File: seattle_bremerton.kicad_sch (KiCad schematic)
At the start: 31 parts

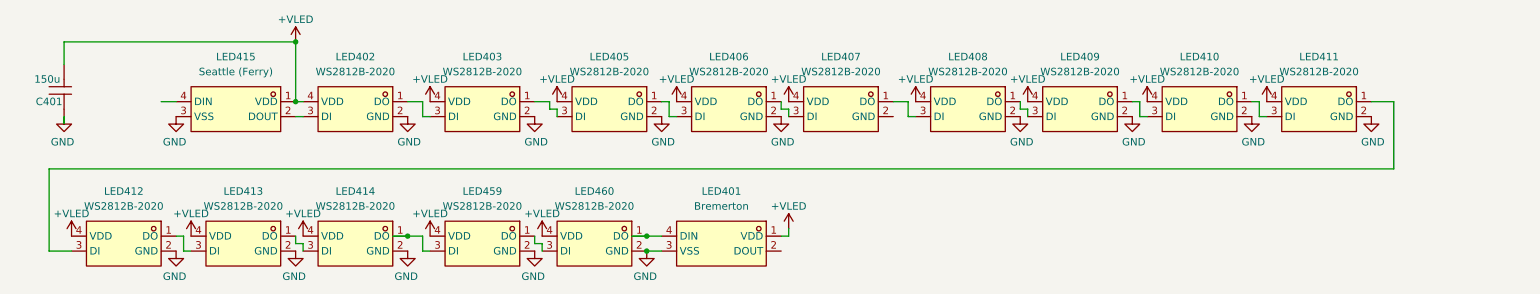
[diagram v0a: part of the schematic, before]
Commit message: checkpoint before stopping double routing
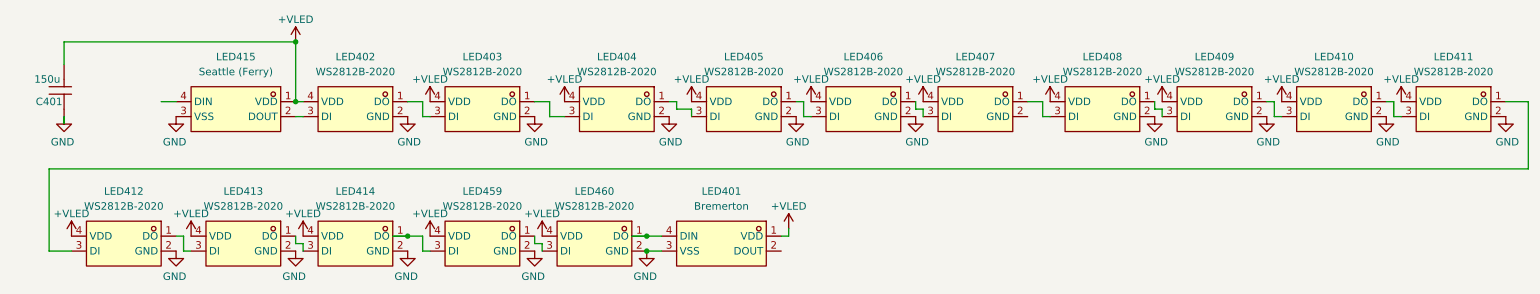
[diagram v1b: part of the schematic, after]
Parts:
- added LED404: WS2812B-2020, EasyEDA:LED-SMD_4P-L2.0-W2.0-TL_WS2812B-2020, symbol EasyEDA:WS2812B-2020
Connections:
- net +VLED: now also LED404.4 (VDD)
- net GND: now also LED404.2 (GND)
- net at LED403.1 (DO): now also LED404.3 (DI); no longer LED405.3 (DI)
- new net: LED404.1 (DO), LED405.3 (DI)
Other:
- moved on the sheet: LED405, LED406, LED407, LED408, LED409, LED410, LED411

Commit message: single ferry track checkpoint
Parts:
- removed LED419, LED430, LED448, LED449, LED450, LED451, LED452, LED453, LED454, LED455, LED456, LED457, LED461, LED462: WS2812B-2020, EasyEDA:LED-SMD_4P-L2.0-W2.0-TL_WS2812B-2020, symbol EasyEDA:WS2812B-2020

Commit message: checkpoint before label plugin
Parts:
- added LED461, LED462: WS2812B-2020, EasyEDA:LED-SMD_4P-L2.0-W2.0-TL_WS2812B-2020, symbol EasyEDA:WS2812B-2020
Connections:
- net +VLED: now also LED461.4 (VDD), LED462.4 (VDD)
- net GND: now also LED461.2 (GND), LED462.2 (GND)
- net at LED460.1 (DO): now also LED461.3 (DI); no longer LED401.4 (DIN)
- new net: LED461.1 (DO), LED462.3 (DI)
- new net: LED401.4 (DIN), LED462.1 (DO)

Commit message: Add rail labels
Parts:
- renumbered LED415 to LED701, LED402 to LED702, LED403 to LED703, LED404 to LED704, LED405 to LED705, LED406 to LED706, LED407 to LED707, LED408 to LED708, LED409 to LED709, LED410 to LED710, LED411 to LED711, LED412 to LED712, LED413 to LED713, LED414 to LED714, LED459 to LED715, LED460 to LED716, LED461 to LED717, LED462 to LED718, LED401 to LED719
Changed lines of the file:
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@@
 		(in_pos_files yes)
 		(dnp no)
-		(property "Reference" "LED461"
+		(property "Reference" "LED717"
 			(at 138.43 52.07 0)
 			(show_name no)
@@
 			(project "transit"
 				(path "/3763eade-a8c8-4ec0-9cf2-9db4442b4ee5/153adc6e-a3b0-4527-a19a-87e28aab4b4d/52f6b4e5-71f2-4ed9-9a18-0787756b3445"
-					(reference "LED461")
+					(reference "LED717")
 					(unit 1)
 				)
@@
 		(in_pos_files yes)
 		(dnp no)
-		(property "Reference" "LED462"
+		(property "Reference" "LED718"
 			(at 157.48 52.07 0)
 			(show_name no)
@@
 			(project "transit"
 				(path "/3763eade-a8c8-4ec0-9cf2-9db4442b4ee5/153adc6e-a3b0-4527-a19a-87e28aab4b4d/52f6b4e5-71f2-4ed9-9a18-0787756b3445"
-					(reference "LED462")
+					(reference "LED718")
 					(unit 1)
 				)
@@
 		(dnp no)
 		(fields_autoplaced yes)
-		(property "Reference" "LED407"
+		(property "Reference" "LED707"
 			(at 181.61 29.21 0)
 			(show_name no)
@@
 			(project "transit"
 				(path "/3763eade-a8c8-4ec0-9cf2-9db4442b4ee5/153adc6e-a3b0-4527-a19a-87e28aab4b4d/52f6b4e5-71f2-4ed9-9a18-0787756b3445"
-					(reference "LED407")
+					(reference "LED707")
 					(unit 1)
 				)
@@
 		(dnp no)
 		(fields_autoplaced yes)
-		(property "Reference" "LED403"
+		(property "Reference" "LED703"
 			(at 97.79 29.21 0)
 			(show_name no)
@@
 			(project "transit"
 				(path "/3763eade-a8c8-4ec0-9cf2-9db4442b4ee5/153adc6e-a3b0-4527-a19a-87e28aab4b4d/52f6b4e5-71f2-4ed9-9a18-0787756b3445"
-					(reference "LED403")
+					(reference "LED703")
 					(unit 1)
 				)
@@
 		(dnp no)
 		(fields_autoplaced yes)
-		(property "Reference" "LED405"
+		(property "Reference" "LED705"
 			(at 142.24 29.21 0)
 			(show_name no)
@@
 			(project "transit"
 				(path "/3763eade-a8c8-4ec0-9cf2-9db4442b4ee5/153adc6e-a3b0-4527-a19a-87e28aab4b4d/52f6b4e5-71f2-4ed9-9a18-0787756b3445"
-					(reference "LED405")
+					(reference "LED705")
 					(unit 1)
 				)
@@
 		(in_pos_files yes)
 		(dnp no)
-		(property "Reference" "LED413"
+		(property "Reference" "LED713"
 			(at 57.15 52.07 0)
 			(show_name no)
@@
 			(project "transit"
 				(path "/3763eade-a8c8-4ec0-9cf2-9db4442b4ee5/153adc6e-a3b0-4527-a19a-87e28aab4b4d/52f6b4e5-71f2-4ed9-9a18-0787756b3445"
-					(reference "LED413")
+					(reference "LED713")
 					(unit 1)
 				)
@@
 		(in_pos_files yes)
 		(dnp no)
-		(property "Reference" "LED414"
+		(property "Reference" "LED714"
 			(at 76.2 52.07 0)
 			(show_name no)
@@
 			(project "transit"
 				(path "/3763eade-a8c8-4ec0-9cf2-9db4442b4ee5/153adc6e-a3b0-4527-a19a-87e28aab4b4d/52f6b4e5-71f2-4ed9-9a18-0787756b3445"
-					(reference "LED414")
+					(reference "LED714")
 					(unit 1)
 				)
@@
 		(in_pos_files yes)
 		(dnp no)
-		(property "Reference" "LED415"
+		(property "Reference" "LED701"
 			(at 55.88 29.21 0)
 			(show_name no)
@@
 			(project "transit"
 				(path "/3763eade-a8c8-4ec0-9cf2-9db4442b4ee5/153adc6e-a3b0-4527-a19a-87e28aab4b4d/52f6b4e5-71f2-4ed9-9a18-0787756b3445"
-					(reference "LED415")
+					(reference "LED701")
 					(unit 1)
 				)
@@
 		(dnp no)
 		(fields_autoplaced yes)
-		(property "Reference" "LED409"
+		(property "Reference" "LED709"
 			(at 222.25 29.21 0)
 			(show_name no)
@@
 			(project "transit"
 				(path "/3763eade-a8c8-4ec0-9cf2-9db4442b4ee5/153adc6e-a3b0-4527-a19a-87e28aab4b4d/52f6b4e5-71f2-4ed9-9a18-0787756b3445"
-					(reference "LED409")
+					(reference "LED709")
 					(unit 1)
 				)
@@
 		(in_pos_files yes)
 		(dnp no)
-		(property "Reference" "LED460"
+		(property "Reference" "LED716"
 			(at 116.84 52.07 0)
 			(show_name no)
@@
 			(project "transit"
 				(path "/3763eade-a8c8-4ec0-9cf2-9db4442b4ee5/153adc6e-a3b0-4527-a19a-87e28aab4b4d/52f6b4e5-71f2-4ed9-9a18-0787756b3445"
-					(reference "LED460")
+					(reference "LED716")
 					(unit 1)
 				)
@@
 		(in_pos_files yes)
 		(dnp no)
-		(property "Reference" "LED402"
+		(property "Reference" "LED702"
 			(at 76.2 29.21 0)
 			(show_name no)
@@
 			(project "transit"
 				(path "/3763eade-a8c8-4ec0-9cf2-9db4442b4ee5/153adc6e-a3b0-4527-a19a-87e28aab4b4d/52f6b4e5-71f2-4ed9-9a18-0787756b3445"
-					(reference "LED402")
+					(reference "LED702")
 					(unit 1)
 				)
@@
 		(in_pos_files yes)
 		(dnp no)
-		(property "Reference" "LED412"
+		(property "Reference" "LED712"
 			(at 36.83 52.07 0)
 			(show_name no)
@@
 			(project "transit"
 				(path "/3763eade-a8c8-4ec0-9cf2-9db4442b4ee5/153adc6e-a3b0-4527-a19a-87e28aab4b4d/52f6b4e5-71f2-4ed9-9a18-0787756b3445"
-					(reference "LED412")
+					(reference "LED712")
 					(unit 1)
 				)
@@
 		(in_pos_files yes)
 		(dnp no)
-		(property "Reference" "LED411"
+		(property "Reference" "LED711"
 			(at 262.89 29.21 0)
 			(show_name no)
@@
 			(project "transit"
 				(path "/3763eade-a8c8-4ec0-9cf2-9db4442b4ee5/153adc6e-a3b0-4527-a19a-87e28aab4b4d/52f6b4e5-71f2-4ed9-9a18-0787756b3445"
-					(reference "LED411")
+					(reference "LED711")
 					(unit 1)
 				)
@@
 		(in_pos_files yes)
 		(dnp no)
-		(property "Reference" "LED459"
+		(property "Reference" "LED715"
 			(at 97.79 52.07 0)
 			(show_name no)
@@
 			(project "transit"
 				(path "/3763eade-a8c8-4ec0-9cf2-9db4442b4ee5/153adc6e-a3b0-4527-a19a-87e28aab4b4d/52f6b4e5-71f2-4ed9-9a18-0787756b3445"
-					(reference "LED459")
+					(reference "LED715")
 					(unit 1)
 				)
@@
 		(dnp no)
 		(fields_autoplaced yes)
-		(property "Reference" "LED406"
+		(property "Reference" "LED706"
 			(at 162.56 29.21 0)
 			(show_name no)
@@
 			(project "transit"
 				(path "/3763eade-a8c8-4ec0-9cf2-9db4442b4ee5/153adc6e-a3b0-4527-a19a-87e28aab4b4d/52f6b4e5-71f2-4ed9-9a18-0787756b3445"
-					(reference "LED406")
+					(reference "LED706")
 					(unit 1)
 				)
@@
 		(dnp no)
 		(fields_autoplaced yes)
-		(property "Reference" "LED410"
+		(property "Reference" "LED710"
 			(at 242.57 29.21 0)
 			(show_name no)
@@
 			(project "transit"
 				(path "/3763eade-a8c8-4ec0-9cf2-9db4442b4ee5/153adc6e-a3b0-4527-a19a-87e28aab4b4d/52f6b4e5-71f2-4ed9-9a18-0787756b3445"
-					(reference "LED410")
+					(reference "LED710")
 					(unit 1)
 				)
@@
 		(dnp no)
 		(fields_autoplaced yes)
-		(property "Reference" "LED408"
+		(property "Reference" "LED708"
 			(at 203.2 29.21 0)
 			(show_name no)
@@
 			(project "transit"
 				(path "/3763eade-a8c8-4ec0-9cf2-9db4442b4ee5/153adc6e-a3b0-4527-a19a-87e28aab4b4d/52f6b4e5-71f2-4ed9-9a18-0787756b3445"
-					(reference "LED408")
+					(reference "LED708")
 					(unit 1)
 				)
@@
 		(dnp no)
 		(fields_autoplaced yes)
-		(property "Reference" "LED404"
+		(property "Reference" "LED704"
 			(at 120.65 29.21 0)
 			(show_name no)
@@
 			(project "transit"
 				(path "/3763eade-a8c8-4ec0-9cf2-9db4442b4ee5/153adc6e-a3b0-4527-a19a-87e28aab4b4d/52f6b4e5-71f2-4ed9-9a18-0787756b3445"
-					(reference "LED404")
+					(reference "LED704")
 					(unit 1)
 				)
@@
 		(in_pos_files yes)
 		(dnp no)
-		(property "Reference" "LED401"
+		(property "Reference" "LED719"
 			(at 180.34 52.07 0)
 			(show_name no)
@@
 			(project "transit"
 				(path "/3763eade-a8c8-4ec0-9cf2-9db4442b4ee5/153adc6e-a3b0-4527-a19a-87e28aab4b4d/52f6b4e5-71f2-4ed9-9a18-0787756b3445"
-					(reference "LED401")
+					(reference "LED719")
 					(unit 1)
 				)

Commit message: junction checkpoint
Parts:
- removed C401: 150u, EasyEDA:CAP-SMD_L3.5-W2.8, symbol EasyEDA:CL21B106KOQNNNE
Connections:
- net at LED703.1 (DO): now also LED701.4 (DIN); no longer LED704.3 (DI)
- net at LED702.1 (DO): now also LED704.3 (DI); no longer LED703.3 (DI)
- net BREMERTON_BAINBRIDGE: now reaches LED719.2 (DOUT)
- new net WT_FERRY_MERGE: LED703.3 (DI)
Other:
- moved on the sheet: LED701, LED702, LED704, LED705, LED706, LED707, LED708, LED709, LED710, LED711, LED712, LED713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

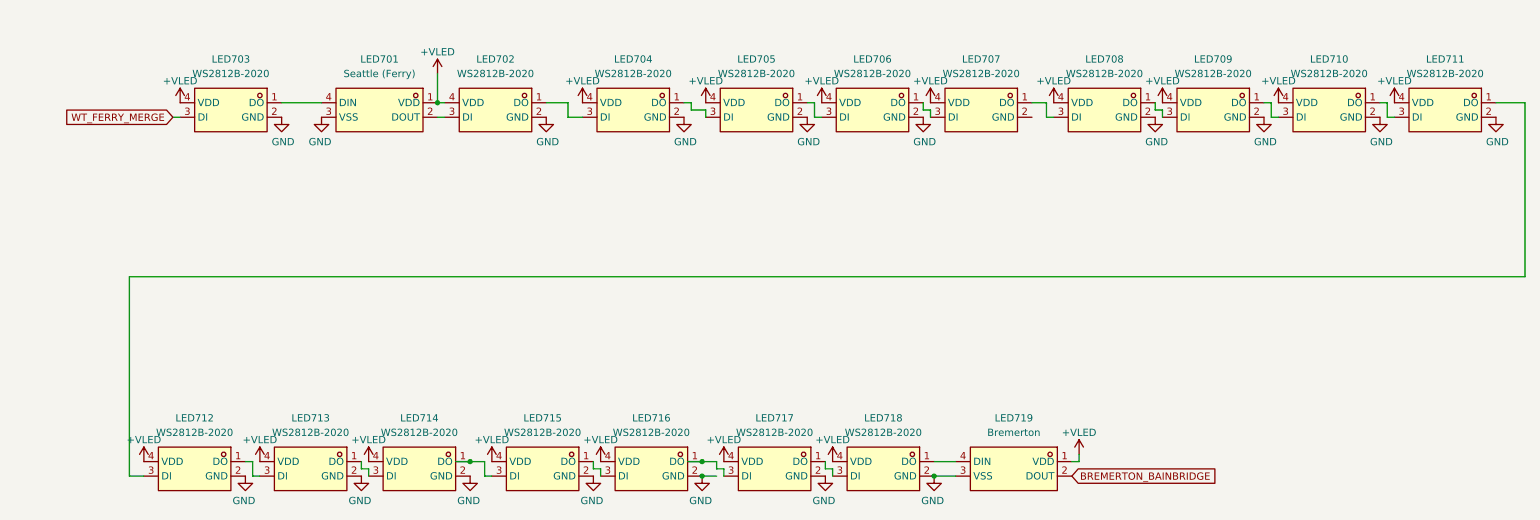
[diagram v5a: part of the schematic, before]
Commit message: reflow reference designators
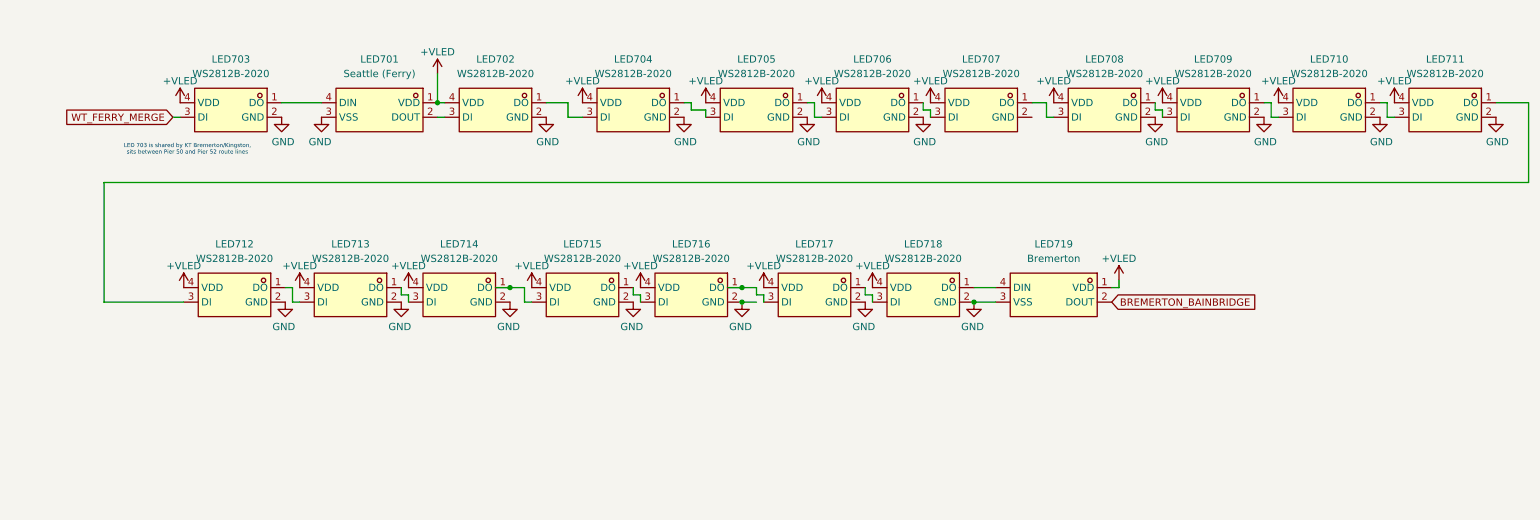
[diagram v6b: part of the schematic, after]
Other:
- note added: "LED 703 is shared by KT Bremerton/Kingston, sits between Pier 50 and Pier 52 route lines"
- moved on the sheet: LED712, LED713, LED714, LED715, LED716, LED717, LED718, LED719
